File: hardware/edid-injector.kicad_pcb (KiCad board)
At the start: 2 copper layers, 42 parts, among them P1 CONN_02X03, SW1 SW_PUSH, U1 C8051F381/3/5/7/C-GQ

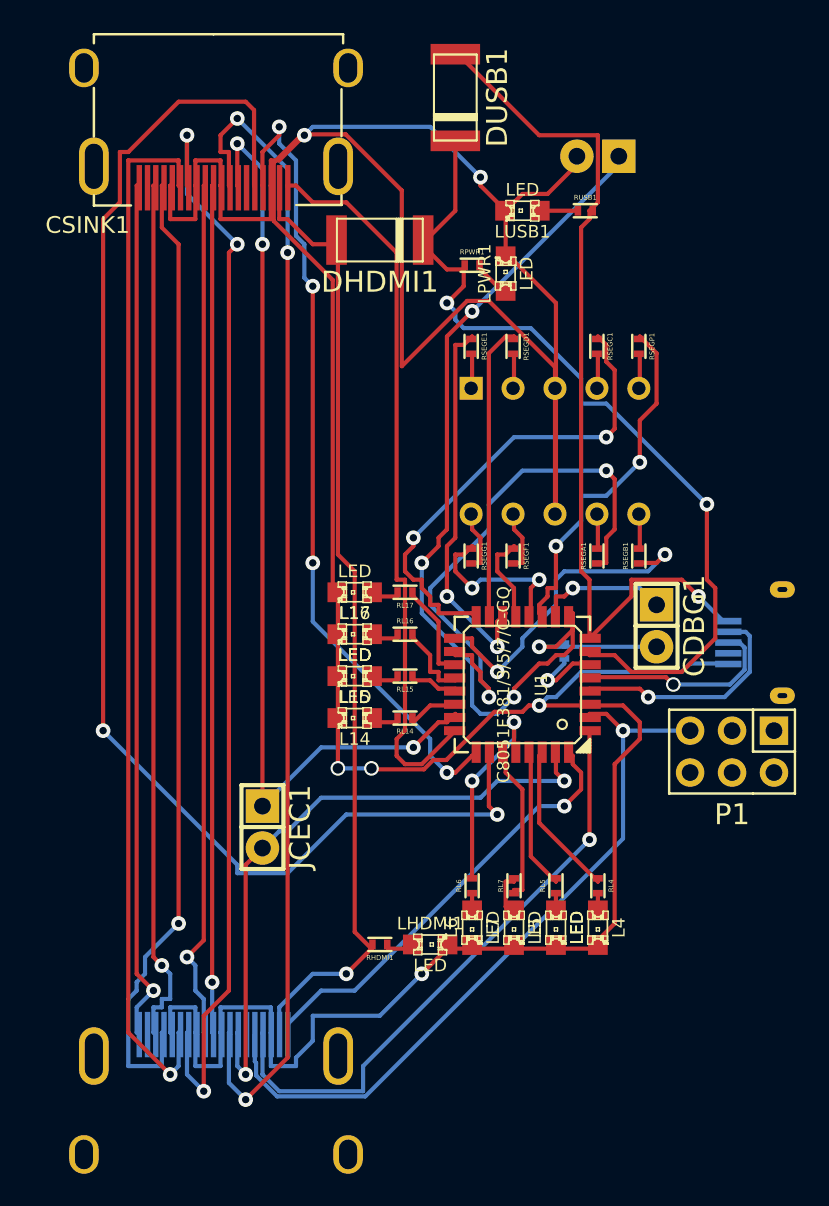
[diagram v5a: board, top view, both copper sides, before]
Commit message: Fixing the EDID jumper.
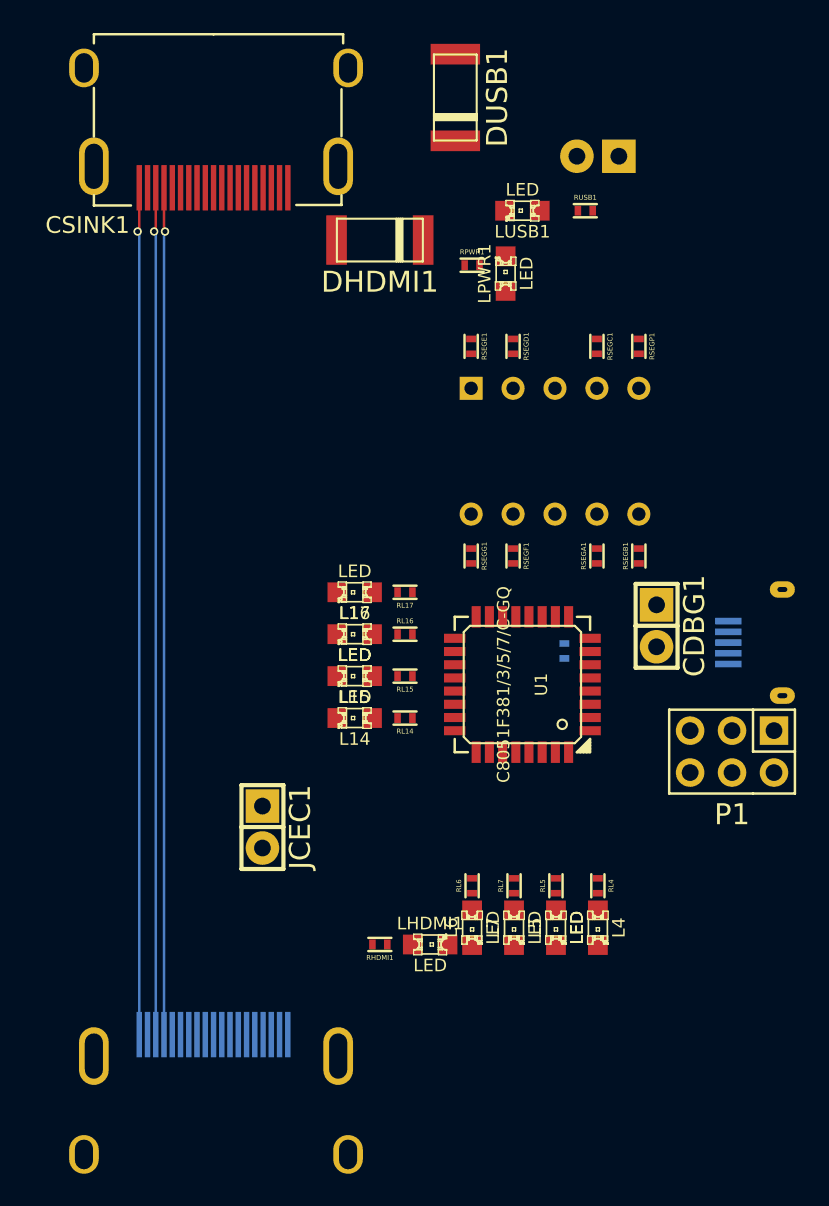
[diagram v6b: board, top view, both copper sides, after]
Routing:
- net GND: track 239.2 -> 0.00 mm, vias 6 -> 0
- net /SINK_SCL: track 83.0 -> 0.00 mm, vias 2 -> 0
- net /CLK-: track 71.5 -> 0.00 mm, vias 3 -> 0
- net /D0+: track 67.4 -> 0.00 mm, vias 3 -> 0
- net /D1-: track 64.1 -> 0.00 mm, vias 1 -> 0
- net Net-(CDBG1-Pad2): track 61.6 -> 0.00 mm, vias 4 -> 0
- net /VHDMI: track 59.6 -> 0.00 mm, vias 1 -> 0
- net /SINK_CEC: track 57.7 -> 0.00 mm, vias 3 -> 0
- net /VUSB: track 54.5 -> 0.00 mm, vias 1 -> 0
- net /VCC5V0: track 53.2 -> 0.00 mm, vias 2 -> 0
- net /D0-: track 52.5 -> 0.00 mm, vias 1 -> 0
- net /CLK+: track 51.6 -> 0.00 mm, vias 1 -> 0
- net /SINK_SDA: track 49.7 -> 0.00 mm, vias 4 -> 0
- net /SRC_SCL: track 45.0 -> 0.00 mm, vias 1 -> 0
- net /SINK_HPD: track 44.3 -> 0.00 mm
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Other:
- net class Default: clearance 0.06 -> 0.2032; trace_width 0.254 -> 0.2032; via_dia 0.889 -> 0.508; via_drill 0.635 -> 0.3048
- net class HighSpeed: clearance 0.06 -> 0.1524; trace_width 0.254 -> 0.1524; via_dia 0.889 -> 0.508; via_drill 0.635 -> 0.3048
- net class PWR: clearance 0.06 -> 0.2032; trace_width 0.254 -> 0.6095; via_dia 0.889 -> 1
- net class SlowSpeed removed
- rule trace_clearance: 0.06 -> 0.2032
- rule trace_min: 0.254 -> 0.1524
- rule via_min_drill: 0.508 -> 0.3048
- rule via_min_size: 0.889 -> 0.508

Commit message: Working on DRC info.
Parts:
- renumbered P1 to JEDID1
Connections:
- JEDID1 pad 1: Net-(P1-Pad1) -> /SRC_HPD
- JEDID1 pad 2: Net-(P1-Pad2) -> /SINK_SCL
- JEDID1 pad 3: Net-(P1-Pad3) -> /SRC_SDA
- JEDID1 pad 4: Net-(P1-Pad4) -> /SINK_SDA
- JEDID1 pad 6: Net-(P1-Pad6) -> /SINK_HPD
- U1 pad 1: /SRC_SDA -> /SRC_SCL
- U1 pad 2: /SRC_SCL -> /SRC_CEC
- U1 pad 23: /SINK_CEC -> /SINK_HPD
- U1 pad 24: /SINK_HPD -> /SINK_SDA
- U1 pad 25: /SINK_SDA -> /SINK_SCL
- U1 pad 26: /SINK_SCL -> /SINK_CEC
- U1 pad 31: /SRC_CEC -> /SRC_HPD
- U1 pad 32: /SRC_HPD -> /SRC_SDA
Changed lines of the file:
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@@
 (kicad_pcb (version 4) (host pcbnew 0.201411141246+5277~19~ubuntu14.04.1-product)
   (general
-    (links 95)
-    (no_connects 95)
-    (area 93.138286 52.898999 141.513058 125.893001)
+    (links 100)
+    (no_connects 97)
+    (area 0 0 0 0)
     (thickness 1.6)
     (drawings 0)
@@
     (zones 0)
     (modules 42)
-    (nets 69)
+    (nets 64)
   )
   (page A4)
@@
   (net 62 "Net-(CSRC1-Pad14)")
   (net 63 "Net-(CUSB1-Pad4)")
-  (net 64 "Net-(P1-Pad1)")
-  (net 65 "Net-(P1-Pad2)")
-  (net 66 "Net-(P1-Pad3)")
-  (net 67 "Net-(P1-Pad4)")
-  (net 68 "Net-(P1-Pad6)")
   (net_class Default "This is the default net class."
     (clearance 0.2032)
@@
     (add_net "Net-(LPWR1-Pad1)")
     (add_net "Net-(LUSB1-Pad1)")
-    (add_net "Net-(P1-Pad1)")
-    (add_net "Net-(P1-Pad2)")
-    (add_net "Net-(P1-Pad3)")
-    (add_net "Net-(P1-Pad4)")
-    (add_net "Net-(P1-Pad6)")
     (add_net "Net-(RL14-Pad1)")
     (add_net "Net-(RL15-Pad1)")
@@
       (net 23 /VUSB))
     (pad 1 smd rect (at -2.79908 4.09956 90) (size 0.55118 1.30048) (layers F.Cu F.Paste F.Mask)
-      (net 19 /SRC_SDA))
+      (net 18 /SRC_SCL))
     (pad 2 smd rect (at -1.99898 4.09956 90) (size 0.55118 1.30048) (layers F.Cu F.Paste F.Mask)
-      (net 18 /SRC_SCL))
+      (net 17 /SRC_CEC))
     (pad 3 smd rect (at -1.19888 4.09956 90) (size 0.55118 1.30048) (layers F.Cu F.Paste F.Mask)
       (net 5 GND))
@@
       (net 39 "Net-(RL14-Pad1)"))
     (pad 23 smd rect (at -1.99898 -4.09956 90) (size 0.55118 1.30048) (layers F.Cu F.Paste F.Mask)
+      (net 16 /SINK_HPD))
+    (pad 24 smd rect (at -2.79908 -4.09956 90) (size 0.55118 1.30048) (layers F.Cu F.Paste F.Mask)
+      (net 14 /SINK_SDA))
+    (pad 25 smd rect (at -4.09956 -2.79908 90) (size 1.30048 0.55118) (layers F.Cu F.Paste F.Mask)
+      (net 13 /SINK_SCL))
+    (pad 26 smd rect (at -4.09956 -1.99898 90) (size 1.30048 0.55118) (layers F.Cu F.Paste F.Mask)
       (net 12 /SINK_CEC))
-    (pad 24 smd rect (at -2.79908 -4.09956 90) (size 0.55118 1.30048) (layers F.Cu F.Paste F.Mask)
-      (net 16 /SINK_HPD))
-    (pad 25 smd rect (at -4.09956 -2.79908 90) (size 1.30048 0.55118) (layers F.Cu F.Paste F.Mask)
-      (net 14 /SINK_SDA))
-    (pad 26 smd rect (at -4.09956 -1.99898 90) (size 1.30048 0.55118) (layers F.Cu F.Paste F.Mask)
-      (net 13 /SINK_SCL))
     (pad 27 smd rect (at -4.09956 -1.19888 90) (size 1.30048 0.55118) (layers F.Cu F.Paste F.Mask)
       (net 38 "Net-(RL7-Pad1)"))
@@
       (net 35 "Net-(RL4-Pad1)"))
     (pad 31 smd rect (at -4.09956 1.99898 90) (size 1.30048 0.55118) (layers F.Cu F.Paste F.Mask)
-      (net 17 /SRC_CEC))
+      (net 20 /SRC_HPD))
     (pad 32 smd rect (at -4.09956 2.79908 90) (size 1.30048 0.55118) (layers F.Cu F.Paste F.Mask)
-      (net 20 /SRC_HPD))
+      (net 19 /SRC_SDA))
     (model smd\smd_lqfp\lqfp-32.wrl
       (at (xyz 0 0 0))
@@
     (descr "Through hole pin header")
     (tags "pin header")
-    (fp_text reference P1 (at 0 -3.81 180) (layer F.SilkS)
+    (fp_text reference JEDID1 (at 0 -3.81 180) (layer F.SilkS)
       (effects (font (size 1.27 1.27) (thickness 0.2032)))
     )
@@
     (fp_line (start -1.27 -2.54) (end -3.81 -2.54) (layer F.SilkS) (width 0.15))
     (pad 1 thru_hole rect (at -2.54 1.27 180) (size 1.7272 1.7272) (drill 1.016) (layers *.Cu *.Mask F.SilkS)
-      (net 64 "Net-(P1-Pad1)"))
+      (net 20 /SRC_HPD))
     (pad 2 thru_hole oval (at -2.54 -1.27 180) (size 1.7272 1.7272) (drill 1.016) (layers *.Cu *.Mask F.SilkS)
-      (net 65 "Net-(P1-Pad2)"))
+      (net 13 /SINK_SCL))
     (pad 3 thru_hole oval (at 0 1.27 180) (size 1.7272 1.7272) (drill 1.016) (layers *.Cu *.Mask F.SilkS)
-      (net 66 "Net-(P1-Pad3)"))
+      (net 19 /SRC_SDA))
     (pad 4 thru_hole oval (at 0 -1.27 180) (size 1.7272 1.7272) (drill 1.016) (layers *.Cu *.Mask F.SilkS)
-      (net 67 "Net-(P1-Pad4)"))
+      (net 14 /SINK_SDA))
     (pad 5 thru_hole oval (at 2.54 1.27 180) (size 1.7272 1.7272) (drill 1.016) (layers *.Cu *.Mask F.SilkS)
       (net 18 /SRC_SCL))
     (pad 6 thru_hole oval (at 2.54 -1.27 180) (size 1.7272 1.7272) (drill 1.016) (layers *.Cu *.Mask F.SilkS)
-      (net 68 "Net-(P1-Pad6)"))
+      (net 16 /SINK_HPD))
     (model Pin_Headers/Pin_Header_Straight_2x03.wrl
       (at (xyz 0 0 0))
@@
     )
   )
+  (via (at 100.778413 67.808) (size 0.508) (drill 0.3048) (layers F.Cu B.Cu) (net 8))
+  (segment (start 100.718 67.868413) (end 100.778413 67.808) (width 0.1524) (layer B.Cu) (net 8))
+  (segment (start 100.718 116.458) (end 100.718 67.868413) (width 0.1524) (layer B.Cu) (net 8))
+  (segment (start 100.718 65.158) (end 100.718 67.747587) (width 0.1524) (layer F.Cu) (net 8))
   (segment (start 100.718 67.747587) (end 100.778413 67.808) (width 0.1524) (layer F.Cu) (net 8))
-  (segment (start 100.718 65.158) (end 100.718 67.747587) (width 0.1524) (layer F.Cu) (net 8))
-  (segment (start 100.718 116.458) (end 100.718 67.868413) (width 0.1524) (layer B.Cu) (net 8))
-  (segment (start 100.718 67.868413) (end 100.778413 67.808) (width 0.1524) (layer B.Cu) (net 8))
-  (via (at 100.778413 67.808) (size 0.508) (drill 0.3048) (layers F.Cu B.Cu) (net 8))
+  (segment (start 100.218 116.458) (end 100.218 67.908) (width 0.1524) (layer B.Cu) (net 9))
+  (via (at 100.118 67.808) (size 0.508) (drill 0.3048) (layers F.Cu B.Cu) (net 9))
+  (segment (start 100.218 65.158) (end 100.218 67.708) (width 0.1524) (layer F.Cu) (net 9))
+  (segment (start 100.218 67.708) (end 100.118 67.808) (width 0.1524) (layer F.Cu) (net 9))
   (segment (start 100.218 67.908) (end 100.118 67.808) (width 0.1524) (layer B.Cu) (net 9))
-  (segment (start 100.218 67.708) (end 100.118 67.808) (width 0.1524) (layer F.Cu) (net 9))
-  (segment (start 100.218 65.158) (end 100.218 67.708) (width 0.1524) (layer F.Cu) (net 9))
-  (via (at 100.118 67.808) (size 0.508) (drill 0.3048) (layers F.Cu B.Cu) (net 9))
-  (segment (start 100.218 116.458) (end 100.218 67.908) (width 0.1524) (layer B.Cu) (net 9))
+  (via (at 99.118 67.808) (size 0.508) (drill 0.3048) (layers F.Cu B.Cu) (net 10))
+  (segment (start 99.218 116.458) (end 99.218 67.858) (width 0.1524) (layer B.Cu) (net 10))
+  (segment (start 99.218 65.158) (end 99.218 67.858) (width 0.1524) (layer F.Cu) (net 10))
+  (segment (start 99.218 67.858) (end 99.168 67.808) (width 0.1524) (layer F.Cu) (net 10))
+  (segment (start 99.168 67.808) (end 99.118 67.808) (width 0.1524) (layer F.Cu) (net 10))
+  (segment (start 99.218 67.858) (end 99.168 67.808) (width 0.1524) (layer B.Cu) (net 10))
   (segment (start 99.168 67.808) (end 99.118 67.808) (width 0.1524) (layer B.Cu) (net 10))
-  (segment (start 99.218 67.858) (end 99.168 67.808) (width 0.1524) (layer B.Cu) (net 10))
-  (segment (start 99.168 67.808) (end 99.118 67.808) (width 0.1524) (layer F.Cu) (net 10))
-  (segment (start 99.218 67.858) (end 99.168 67.808) (width 0.1524) (layer F.Cu) (net 10))
-  (segment (start 99.218 65.158) (end 99.218 67.858) (width 0.1524) (layer F.Cu) (net 10))
-  (segment (start 99.218 116.458) (end 99.218 67.858) (width 0.1524) (layer B.Cu) (net 10))
-  (via (at 99.118 67.808) (size 0.508) (drill 0.3048) (layers F.Cu B.Cu) (net 10))
 )

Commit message: Update PCB
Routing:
- net /D1-: track 0.00 -> 51.4 mm, vias 0 -> 1
- net /D0-: track 0.00 -> 51.4 mm, vias 0 -> 1
- net /CLK-: track 0.00 -> 51.4 mm, vias 0 -> 1
- net /CLK+: track 0.00 -> 51.4 mm, vias 0 -> 1
- net /D0+: track 0.00 -> 51.4 mm, vias 0 -> 1
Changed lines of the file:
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@@
-(kicad_pcb (version 4) (host pcbnew 0.201411141246+5277~19~ubuntu14.04.1-product)
+(kicad_pcb (version 4) (host pcbnew "(2014-jul-16 BZR unknown)-product")
   (general
     (links 100)
-    (no_connects 97)
-    (area 0 0 0 0)
+    (no_connects 100)
+    (area 92.71 52.07 142.24 125.73)
     (thickness 1.6)
     (drawings 0)
-    (tracks 17)
+    (tracks 67)
     (zones 0)
     (modules 42)
@@
     (pad_to_mask_clearance 0)
     (aux_axis_origin 0 0)
-    (grid_origin 175.768 121.158)
+    (grid_origin 99.187 66.548)
     (visible_elements FFFFFF7F)
     (pcbplotparams
@@
     )
   )
-  (via (at 100.778413 67.808) (size 0.508) (drill 0.3048) (layers F.Cu B.Cu) (net 8))
-  (segment (start 100.718 67.868413) (end 100.778413 67.808) (width 0.1524) (layer B.Cu) (net 8))
-  (segment (start 100.718 116.458) (end 100.718 67.868413) (width 0.1524) (layer B.Cu) (net 8))
-  (segment (start 100.718 65.158) (end 100.718 67.747587) (width 0.1524) (layer F.Cu) (net 8))
-  (segment (start 100.718 67.747587) (end 100.778413 67.808) (width 0.1524) (layer F.Cu) (net 8))
-  (segment (start 100.218 116.458) (end 100.218 67.908) (width 0.1524) (layer B.Cu) (net 9))
-  (via (at 100.118 67.808) (size 0.508) (drill 0.3048) (layers F.Cu B.Cu) (net 9))
-  (segment (start 100.218 65.158) (end 100.218 67.708) (width 0.1524) (layer F.Cu) (net 9))
-  (segment (start 100.218 67.708) (end 100.118 67.808) (width 0.1524) (layer F.Cu) (net 9))
-  (segment (start 100.218 67.908) (end 100.118 67.808) (width 0.1524) (layer B.Cu) (net 9))
-  (via (at 99.118 67.808) (size 0.508) (drill 0.3048) (layers F.Cu B.Cu) (net 10))
-  (segment (start 99.218 116.458) (end 99.218 67.858) (width 0.1524) (layer B.Cu) (net 10))
-  (segment (start 99.218 65.158) (end 99.218 67.858) (width 0.1524) (layer F.Cu) (net 10))
-  (segment (start 99.218 67.858) (end 99.168 67.808) (width 0.1524) (layer F.Cu) (net 10))
-  (segment (start 99.168 67.808) (end 99.118 67.808) (width 0.1524) (layer F.Cu) (net 10))
-  (segment (start 99.218 67.858) (end 99.168 67.808) (width 0.1524) (layer B.Cu) (net 10))
-  (segment (start 99.168 67.808) (end 99.118 67.808) (width 0.1524) (layer B.Cu) (net 10))
+  (segment (start 103.717 66.738) (end 103.718 66.737) (width 0.1524) (layer F.Cu) (net 3))
+  (segment (start 103.718 66.737) (end 103.718 65.158) (width 0.1524) (layer F.Cu) (net 3))
+  (segment (start 103.817 66.838) (end 103.717 66.738) (width 0.1524) (layer F.Cu) (net 3))
+  (segment (start 103.817 67.538) (end 103.817 66.838) (width 0.1524) (layer F.Cu) (net 3))
+  (segment (start 103.817 114.74) (end 103.817 67.538) (width 0.1524) (layer B.Cu) (net 3))
+  (via (at 103.817 67.538) (size 0.508) (drill 0.3048) (layers F.Cu B.Cu) (net 3))
+  (segment (start 103.718 114.839) (end 103.817 114.74) (width 0.1524) (layer B.Cu) (net 3))
+  (segment (start 103.718 116.458) (end 103.718 114.839) (width 0.1524) (layer B.Cu) (net 3))
+  (segment (start 103.117 67.538) (end 103.117 114.738) (width 0.1524) (layer B.Cu) (net 4))
+  (segment (start 103.117 114.738) (end 103.218 114.839) (width 0.1524) (layer B.Cu) (net 4))
+  (segment (start 103.218 114.839) (end 103.218 116.458) (width 0.1524) (layer B.Cu) (net 4))
+  (segment (start 103.117 66.838) (end 103.117 67.538) (width 0.1524) (layer F.Cu) (net 4))
+  (via (at 103.117 67.538) (size 0.508) (drill 0.3048) (layers F.Cu B.Cu) (net 4))
+  (segment (start 103.218 66.737) (end 103.117 66.838) (width 0.1524) (layer F.Cu) (net 4))
+  (segment (start 103.218 65.158) (end 103.218 66.737) (width 0.1524) (layer F.Cu) (net 4))
+  (segment (start 102.317 114.74) (end 102.317 70.538) (width 0.1524) (layer B.Cu) (net 6))
+  (segment (start 102.317 70.538) (end 102.317 67.538) (width 0.1524) (layer B.Cu) (net 6))
+  (segment (start 102.218 114.839) (end 102.317 114.74) (width 0.1524) (layer B.Cu) (net 6))
+  (segment (start 102.218 116.458) (end 102.218 114.839) (width 0.1524) (layer B.Cu) (net 6))
+  (segment (start 102.317 66.836) (end 102.317 67.538) (width 0.1524) (layer F.Cu) (net 6))
+  (via (at 102.317 67.538) (size 0.508) (drill 0.3048) (layers F.Cu B.Cu) (net 6))
+  (segment (start 102.218 66.737) (end 102.317 66.836) (width 0.1524) (layer F.Cu) (net 6))
+  (segment (start 102.218 65.158) (end 102.218 66.737) (width 0.1524) (layer F.Cu) (net 6))
+  (segment (start 101.717 66.738) (end 101.617 66.838) (width 0.1524) (layer F.Cu) (net 7))
+  (segment (start 101.617 66.838) (end 101.617 67.538) (width 0.1524) (layer F.Cu) (net 7))
+  (segment (start 101.717 66.6864) (end 101.717 66.738) (width 0.1524) (layer F.Cu) (net 7))
+  (segment (start 101.718 65.158) (end 101.718 66.6854) (width 0.1524) (layer F.Cu) (net 7))
+  (segment (start 101.718 66.6854) (end 101.717 66.6864) (width 0.1524) (layer F.Cu) (net 7))
+  (segment (start 101.617 67.538) (end 101.617 114.738) (width 0.1524) (layer B.Cu) (net 7))
+  (segment (start 101.717 115.138) (end 101.718 115.139) (width 0.1524) (layer B.Cu) (net 7))
+  (segment (start 101.617 114.738) (end 101.717 114.838) (width 0.1524) (layer B.Cu) (net 7))
+  (segment (start 101.717 114.838) (end 101.717 115.138) (width 0.1524) (layer B.Cu) (net 7))
+  (segment (start 101.718 115.139) (end 101.718 116.458) (width 0.1524) (layer B.Cu) (net 7))
+  (via (at 101.617 67.538) (size 0.508) (drill 0.3048) (layers F.Cu B.Cu) (net 7))
+  (segment (start 100.817 66.836) (end 100.817 67.538) (width 0.1524) (layer F.Cu) (net 8))
+  (segment (start 100.718 66.737) (end 100.817 66.836) (width 0.1524) (layer F.Cu) (net 8))
+  (segment (start 100.718 65.158) (end 100.718 66.737) (width 0.1524) (layer F.Cu) (net 8))
+  (segment (start 100.817 114.738) (end 100.817 84.738) (width 0.1524) (layer B.Cu) (net 8))
+  (segment (start 100.817 84.738) (end 100.817 67.538) (width 0.1524) (layer B.Cu) (net 8))
+  (segment (start 100.718 114.837) (end 100.817 114.738) (width 0.1524) (layer B.Cu) (net 8))
+  (segment (start 100.718 114.9306) (end 100.718 114.837) (width 0.1524) (layer B.Cu) (net 8))
+  (segment (start 100.718 116.458) (end 100.718 114.9306) (width 0.1524) (layer B.Cu) (net 8))
+  (segment (start 100.718 114.9306) (end 100.717 114.9296) (width 0.1524) (layer B.Cu) (net 8))
+  (via (at 100.817 67.538) (size 0.508) (drill 0.3048) (layers F.Cu B.Cu) (net 8))
+  (segment (start 100.117 66.838) (end 100.117 67.538) (width 0.1524) (layer F.Cu) (net 9))
+  (segment (start 100.218 66.737) (end 100.117 66.838) (width 0.1524) (layer F.Cu) (net 9))
+  (segment (start 100.218 65.158) (end 100.218 66.737) (width 0.1524) (layer F.Cu) (net 9))
+  (segment (start 100.117 67.538) (end 100.117 114.738) (width 0.1524) (layer B.Cu) (net 9))
+  (segment (start 100.117 114.738) (end 100.218 114.839) (width 0.1524) (layer B.Cu) (net 9))
+  (segment (start 100.218 114.839) (end 100.218 116.458) (width 0.1524) (layer B.Cu) (net 9))
+  (via (at 100.117 67.538) (size 0.508) (drill 0.3048) (layers F.Cu B.Cu) (net 9))
+  (segment (start 99.317 114.138) (end 99.317 67.538) (width 0.1524) (layer B.Cu) (net 10))
+  (segment (start 99.317 114.74) (end 99.317 114.138) (width 0.1524) (layer B.Cu) (net 10))
+  (segment (start 99.218 114.839) (end 99.317 114.74) (width 0.1524) (layer B.Cu) (net 10))
+  (segment (start 99.218 116.458) (end 99.218 114.839) (width 0.1524) (layer B.Cu) (net 10))
+  (segment (start 99.317 66.836) (end 99.317 67.538) (width 0.1524) (layer F.Cu) (net 10))
+  (segment (start 99.218 66.737) (end 99.317 66.836) (width 0.1524) (layer F.Cu) (net 10))
+  (segment (start 99.218 65.158) (end 99.218 66.737) (width 0.1524) (layer F.Cu) (net 10))
+  (via (at 99.317 67.538) (size 0.508) (drill 0.3048) (layers F.Cu B.Cu) (net 10))
+  (segment (start 99.217 116.457) (end 99.218 116.458) (width 0.1524) (layer B.Cu) (net 10))
+  (segment (start 104.617 67.538) (end 104.617 114.738) (width 0.1524) (layer B.Cu) (net 11))
+  (segment (start 104.617 114.738) (end 104.718 114.839) (width 0.1524) (layer B.Cu) (net 11))
+  (segment (start 104.718 114.839) (end 104.718 116.458) (width 0.1524) (layer B.Cu) (net 11))
+  (segment (start 104.617 66.838) (end 104.617 67.538) (width 0.1524) (layer F.Cu) (net 11))
+  (via (at 104.617 67.538) (size 0.508) (drill 0.3048) (layers F.Cu B.Cu) (net 11))
+  (segment (start 104.718 66.737) (end 104.617 66.838) (width 0.1524) (layer F.Cu) (net 11))
+  (segment (start 104.718 65.158) (end 104.718 66.737) (width 0.1524) (layer F.Cu) (net 11))
 )
